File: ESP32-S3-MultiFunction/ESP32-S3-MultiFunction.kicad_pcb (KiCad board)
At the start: 2 copper layers, 99.1 x 125.7 mm, 152 parts, among them IC1 ESP32-S3FN8, IC2 USBLC6-2SC6, J1 USB_OTG, J501 -SM+, J801 RJ45, J802 RJ45, P701 A7 A6 A5 A4 A3 A2 A1 A0 C, P702 B7 B6 B5 B4 B3 B2 B1 B0 C, SW1 BOOT, SW201 RESET, T701 + 12V -, T801 - 15 in +, T802 - 15 out +, U301 LM2574N-3.3, U401 TC4426, U402 TC4426, U403 74HCT14, U501 74HCT00, U502 74HCT00, U503 TC4428, U504 TC4428, U505 TC4428, U506 TC4428, U601 LM339, U602 LM339, U701 PCA9685, U702 TBD62X83A, U703 TBD62X83A, U801 TCAN332DR, Y201 40 Mhz +/- 10 ppm

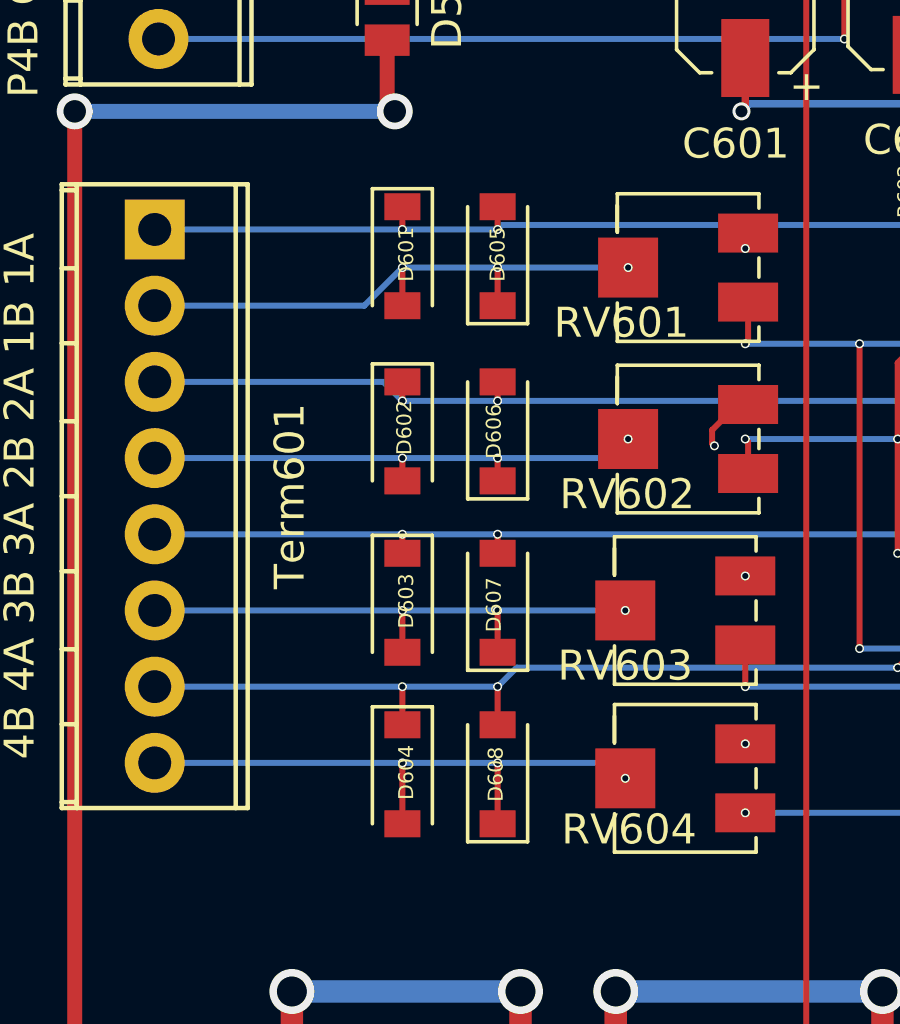
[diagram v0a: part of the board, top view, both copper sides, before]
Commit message: Fix footprint for OC Diodes.
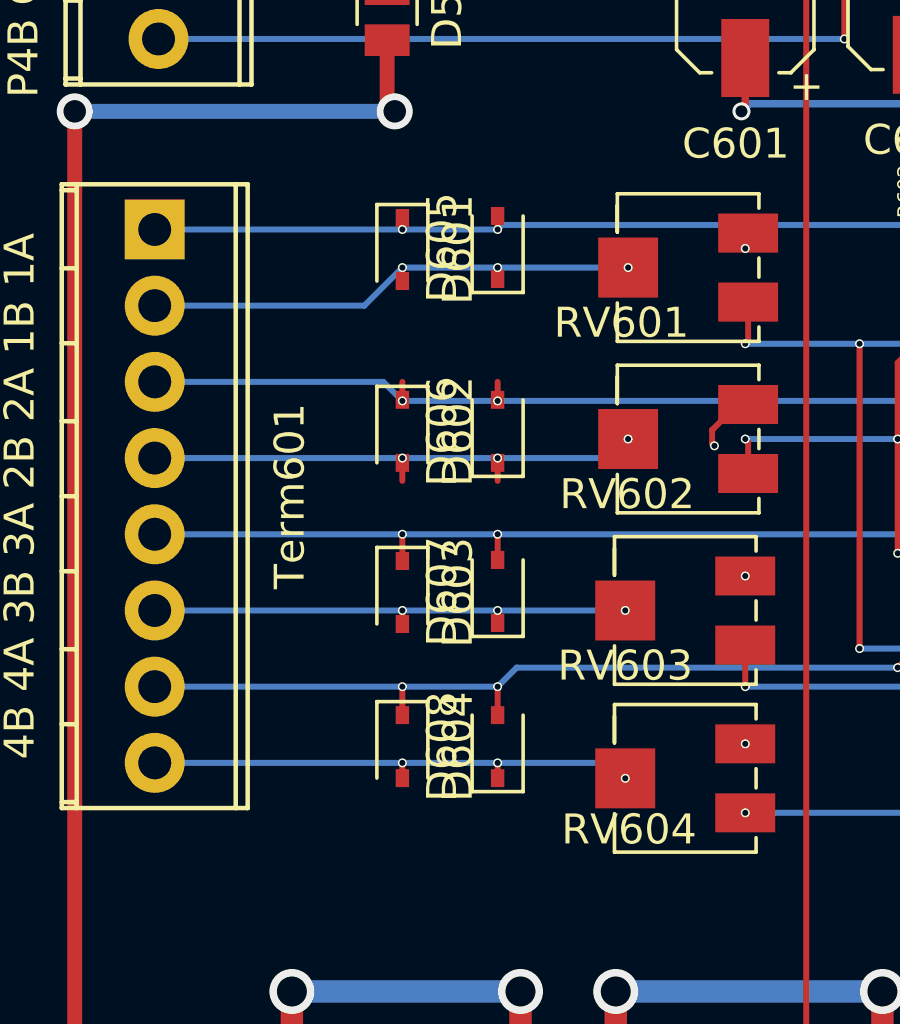
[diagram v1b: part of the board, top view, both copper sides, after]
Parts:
- D601, D602, D603, D604, D605, D606, D607, D608: footprint Diodes_SMD:D_SOD-123 -> Diodes_SMD:D_SOD-323
- moved D604 0.92 mm to (88.1, 118.2)
- moved D608 0.92 mm to (91.3, 118.2)
- moved D607 0.38 mm to (91.3, 113.0)
- moved D603 0.35 mm to (88.1, 113.1)
- moved D605 0.29 mm to (91.3, 101.6)
- moved D601 0.22 mm to (88.1, 101.6)
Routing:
- net Net-(D604-Pad2): track 20.0 -> 16.9 mm
- net Net-(D603-Pad2): track 18.5 -> 16.5 mm
- net Net-(D601-Pad2): track 18.8 -> 17.1 mm
- net Net-(D601-Pad1): track 33.1 -> 32.4 mm
- net Net-(D604-Pad1): track 35.7 -> 35.1 mm

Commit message: WROOM module Version.
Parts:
- removed C201, C202: 10uf, Capacitors_SMD:C_0805
- removed C203, C206, C217: 1uf, Capacitors_SMD:C_0402
- removed C204, C205, C208: 100nf, Capacitors_SMD:C_0402
- removed C207: 100pf, Capacitors_SMD:C_0402
- removed C215, C216: 22pf, Capacitors_SMD:C_0402
- removed L201: 2.0nH, Inductors_SMD:L_0402
- removed R1: 0, Resistors_SMD:R_0402
- removed Y201: 40 Mhz +/- 10 ppm, FA_20H:FA20_H
- IC1: value ESP32-S3FN8 -> ESP32-S3-WROOM-1U-N8; footprint Housings_DFN_QFN:QFN-56-1EP_7x7mm_Pitch0.4mm -> ESP32-S3-WROOM:ESP32_S3_WROOM-1U
- moved FD103 126.5 mm to (123.2, 161.2)
- moved REF*** 16.3 mm to (132.7, 67.9)
- moved IC1 8.43 mm to (115.8, 53.7), turned to 0 degrees
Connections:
- D609 pad 1: /ESP32 MCU/GPIO34(OD1) -> /ESP32 MCU/GPIO40(OD1)
- IC1 pad 1: Net-(IC1-Pad1) -> GND
- IC1 pad 10: /CAN Tranceiver/CAN_TX -> /ESP32 MCU/GPIO17(LEDS1)
- IC1 pad 11: /Buttons and LEDs/Button2 -> /ESP32 MCU/GPIO18(LEDS2)
- IC1 pad 12: /ESP32 MCU/GPIO7(OD4) -> /ESP32 MCU/GPIO8(Motor3)
- IC1 pad 13: /ESP32 MCU/GPIO8(Motor3) -> /ESP32 MCU/D-
- IC1 pad 14: /ESP32 MCU/GPIO9(Motor1) -> /ESP32 MCU/D+
- IC1 pad 15: /ESP32 MCU/GPIO10(Points4) -> /ESP32 MCU/SCL
- IC1 pad 16: /ESP32 MCU/GPIO11(Motor2) -> Net-(IC1-Pad16)
- IC1 pad 17: /ESP32 MCU/GPIO12(Points1) -> /ESP32 MCU/GPIO9(Motor1)
- IC1 pad 18: /ESP32 MCU/GPIO13(Points2) -> /ESP32 MCU/GPIO10(Points4)
- IC1 pad 19: /ESP32 MCU/GPIO14(Points3) -> /ESP32 MCU/GPIO11(Motor2)
- IC1 pad 2: /ESP32 MCU/VDD3P3 -> +3V3
- IC1 pad 20: +3V3 -> /ESP32 MCU/GPIO12(Points1)
- IC1 pad 21: /ESP32 MCU/GPIO15(Act1) -> /ESP32 MCU/GPIO13(Points2)
- IC1 pad 22: /Buttons and LEDs/Button4 -> /ESP32 MCU/GPIO14(Points3)
- IC1 pad 23: /ESP32 MCU/GPIO17(LEDS1) -> /ESP32 MCU/GPIO21(LEDS3)
- IC1 pad 24: /ESP32 MCU/GPIO18(LEDS2) -> Net-(IC1-Pad24)
- IC1 pad 25: /ESP32 MCU/D- -> Net-(IC1-Pad25)
- IC1 pad 26: /ESP32 MCU/D+ -> Net-(IC1-Pad26)
- IC1 pad 27: /ESP32 MCU/GPIO21(LEDS3) -> /ESP32 MCU/GPIO0(Act2)
- IC1 pad 28: Net-(IC1-Pad28) -> /ESP32 MCU/GPIO35(OD2)
- IC1 pad 29: Net-(C217-Pad1) -> /ESP32 MCU/GPIO36(OD3)
- IC1 pad 3: /ESP32 MCU/VDD3P3 -> /ESP32 MCU/RESET
- IC1 pad 30: Net-(IC1-Pad30) -> /Buttons and LEDs/Button3
- IC1 pad 31: Net-(IC1-Pad31) -> /Buttons and LEDs/Button1
- IC1 pad 32: Net-(IC1-Pad32) -> /ESP32 MCU/GPIO39(Motor4)
- IC1 pad 33: Net-(IC1-Pad33) -> /ESP32 MCU/GPIO40(OD1)
- IC1 pad 38: /ESP32 MCU/GPIO33(Motor4) -> /ESP32 MCU/SDA
- IC1 pad 39: /ESP32 MCU/GPIO34(OD1) -> /ESP32 MCU/GPIO1(LEDS4)
- IC1 pad 4: /ESP32 MCU/RESET -> /CAN Tranceiver/CAN_RX
- IC1 pad 40: /ESP32 MCU/GPIO35(OD2) -> GND
- IC1 pad 5: /ESP32 MCU/GPIO0(Act2) -> /CAN Tranceiver/CAN_TX
- IC1 pad 6: /ESP32 MCU/GPIO1(LEDS4) -> /Buttons and LEDs/Button2
- IC1 pad 7: /ESP32 MCU/SDA -> /ESP32 MCU/GPIO7(OD4)
- IC1 pad 8: /ESP32 MCU/SCL -> /ESP32 MCU/GPIO15(Act1)
- IC1 pad 9: /CAN Tranceiver/CAN_RX -> /Buttons and LEDs/Button4
- U506 pad 2: /ESP32 MCU/GPIO33(Motor4) -> /ESP32 MCU/GPIO39(Motor4)
- U506 pad 4: /ESP32 MCU/GPIO33(Motor4) -> /ESP32 MCU/GPIO39(Motor4)
- U602 pad 2: /ESP32 MCU/GPIO34(OD1) -> /ESP32 MCU/GPIO40(OD1)
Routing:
- net /ESP32 MCU/GPIO34(OD1): track 96.3 -> 0.00 mm, vias 8 -> 0
- net /ESP32 MCU/GPIO8(Motor3): track 117.5 -> 31.6 mm, vias 4 -> 2
- net /ESP32 MCU/GPIO33(Motor4): track 78.7 -> 0.00 mm, vias 2 -> 0
- net /ESP32 MCU/GPIO40(OD1): track 0.00 -> 77.1 mm, vias 0 -> 6
- net /ESP32 MCU/GPIO18(LEDS2): track 200.0 -> 124.4 mm, vias 8 -> 6
- net /ESP32 MCU/GPIO39(Motor4): track 0.00 -> 70.0 mm, vias 0 -> 4
- net /ESP32 MCU/GPIO17(LEDS1): track 175.7 -> 108.7 mm, vias 6 -> 4
- net /ESP32 MCU/GPIO11(Motor2): track 88.0 -> 47.6 mm, vias 4 -> 2
- net /ESP32 MCU/SCL: track 44.3 -> 83.8 mm, vias 4 -> 7
- net /ESP32 MCU/GPIO10(Points4): track 72.6 -> 36.0 mm, vias 5 -> 3
- net /ESP32 MCU/D-: track 8.53 -> 40.8 mm, vias 0 -> 2
- net /ESP32 MCU/D+: track 8.62 -> 40.6 mm, vias 0 -> 2
- net /ESP32 MCU/GPIO14(Points3): track 61.1 -> 30.0 mm, vias 4 -> 3
- net /Buttons and LEDs/Button3: track 136.3 -> 108.1 mm, vias 6 -> 4
- net /ESP32 MCU/GPIO21(LEDS3): track 122.0 -> 93.8 mm, vias 6 -> 4
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
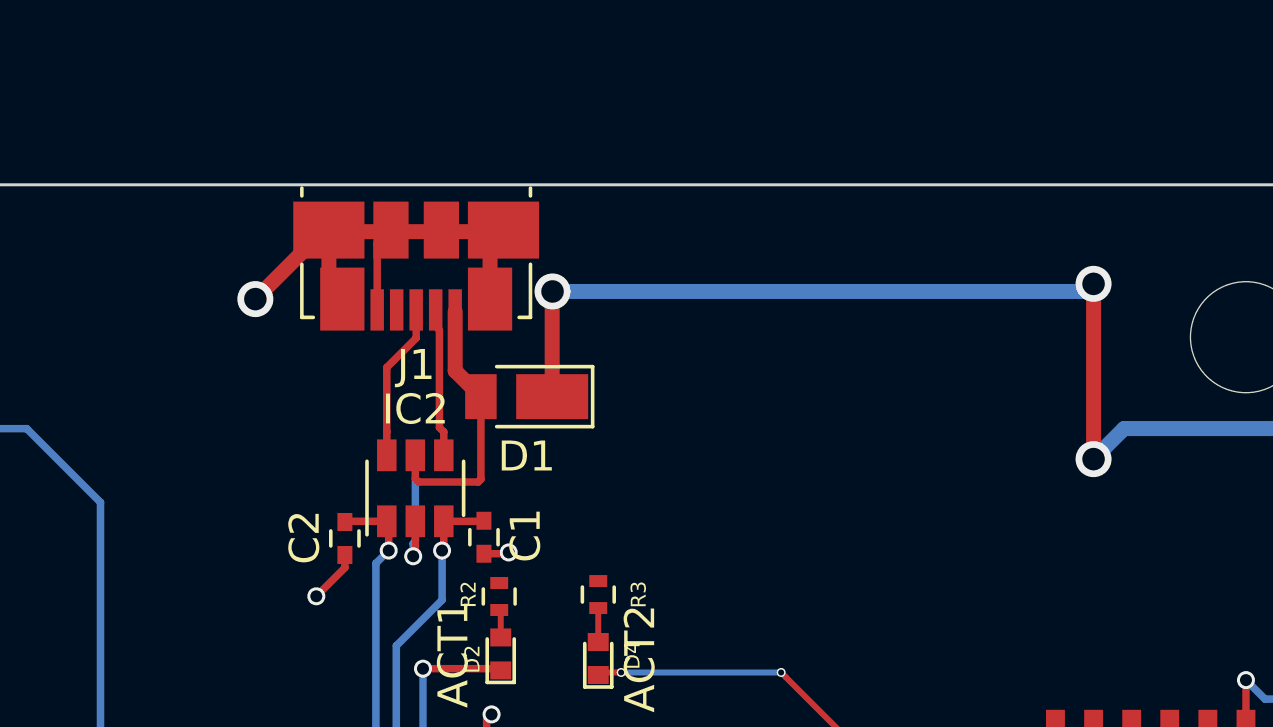
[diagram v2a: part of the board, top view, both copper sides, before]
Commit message: Change USB-MicroB to USB-C.
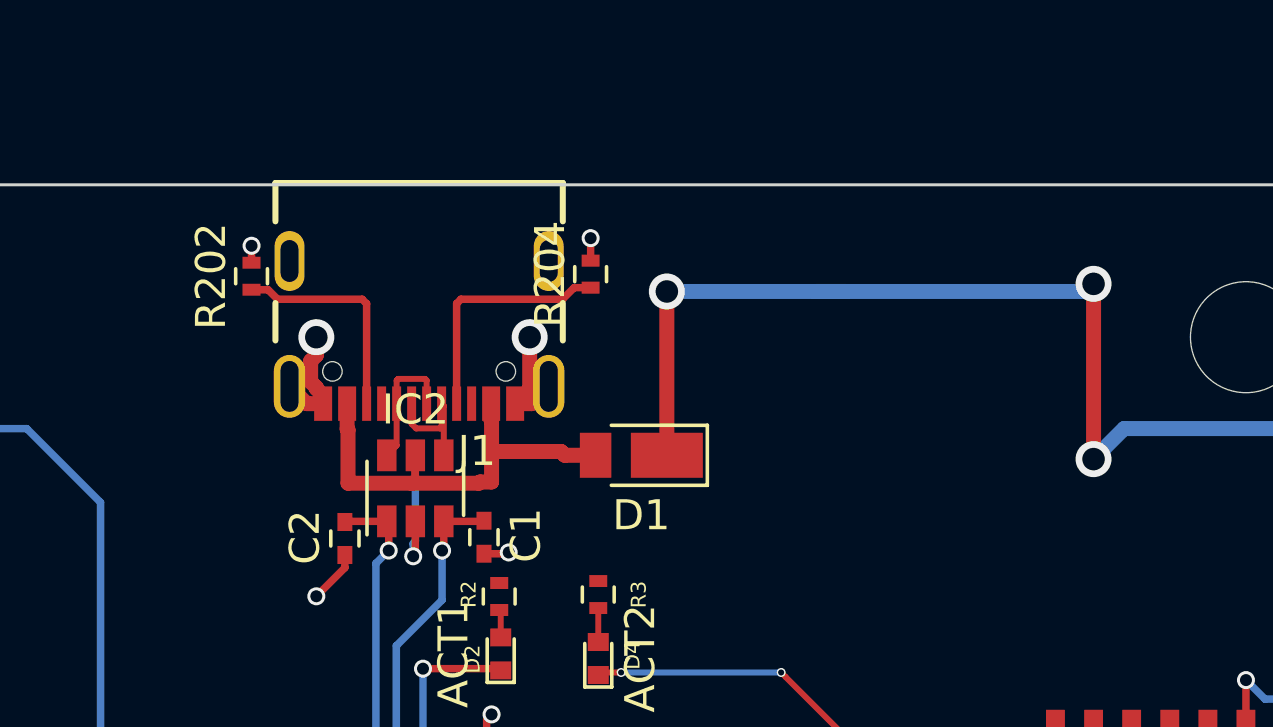
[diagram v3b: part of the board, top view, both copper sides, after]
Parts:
- added R202: 5.1K, Resistors_SMD:R_0402, F.Cu at (116.7, 28.4)
- added R204: 5.1K, Resistors_SMD:R_0402, F.Cu at (128.0, 28.4)
- J1: value USB_OTG -> USB_C; footprint Connectors_USB:USB_Micro-B_Molex_47346-0001 -> GCT_USB:GCT_USB4105-GF-A
- moved D1 4.29 mm to (129.7, 34.4)
- moved J1 1.03 mm to (122.3, 27.9)
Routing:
- net GND: track 142.2 -> 134.0 mm, vias 54 -> 57
- net Net-(J1-PadA5): track 0.00 -> 8.02 mm
- net Net-(J1-PadB5): track 0.00 -> 7.36 mm
- net VBUS: track 9.14 -> 15.4 mm
- net Net-(IC2-Pad6): track 5.48 -> 4.45 mm
- net Net-(C302-Pad1): track 181.7 -> 180.8 mm
- net Net-(IC2-Pad4): track 4.96 -> 4.28 mm

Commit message: Update to new PBs.
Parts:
- SW1, SW201: footprint PTS647SN70SMTR2LFS:PTS647SM38SMTR2LFS -> Buttons_Switches_SMD:SW_SPST_B3U-1000P-B
- moved SW1 4.13 mm to (131.7, 58.1)
- moved SW201 1.69 mm to (127.1, 58.0)
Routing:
- net /ESP32 MCU/GPIO0(Act2): track 42.1 -> 48.4 mm
- net /Buttons and LEDs/Button3: track 108.1 -> 109.3 mm
- net /ESP32 MCU/RESET: track 33.7 -> 34.4 mm
